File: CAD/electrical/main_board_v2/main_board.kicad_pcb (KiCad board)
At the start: 2 copper layers, 85.7 x 55.2 mm, 45 parts, among them J1 Battery in, J10 I2C Motor, J11 JTAG, J12 UART PGM, J2 Raspberry_Pi_2_3_4, J3 Trigger, J4 Side select, J5 Button A, J6 Button B, J7 I2C Peripheral, J8 I2C Peripheral, J9 I2C Motor, SW1 RESET, SW2 BOOT, U1 LM2576S-5, U2 AMS1117-3.3, U3 ESP32-WROOM-32, U4 PCA9306DC1, U5 PCA9306DC1, U6 MPU-6050

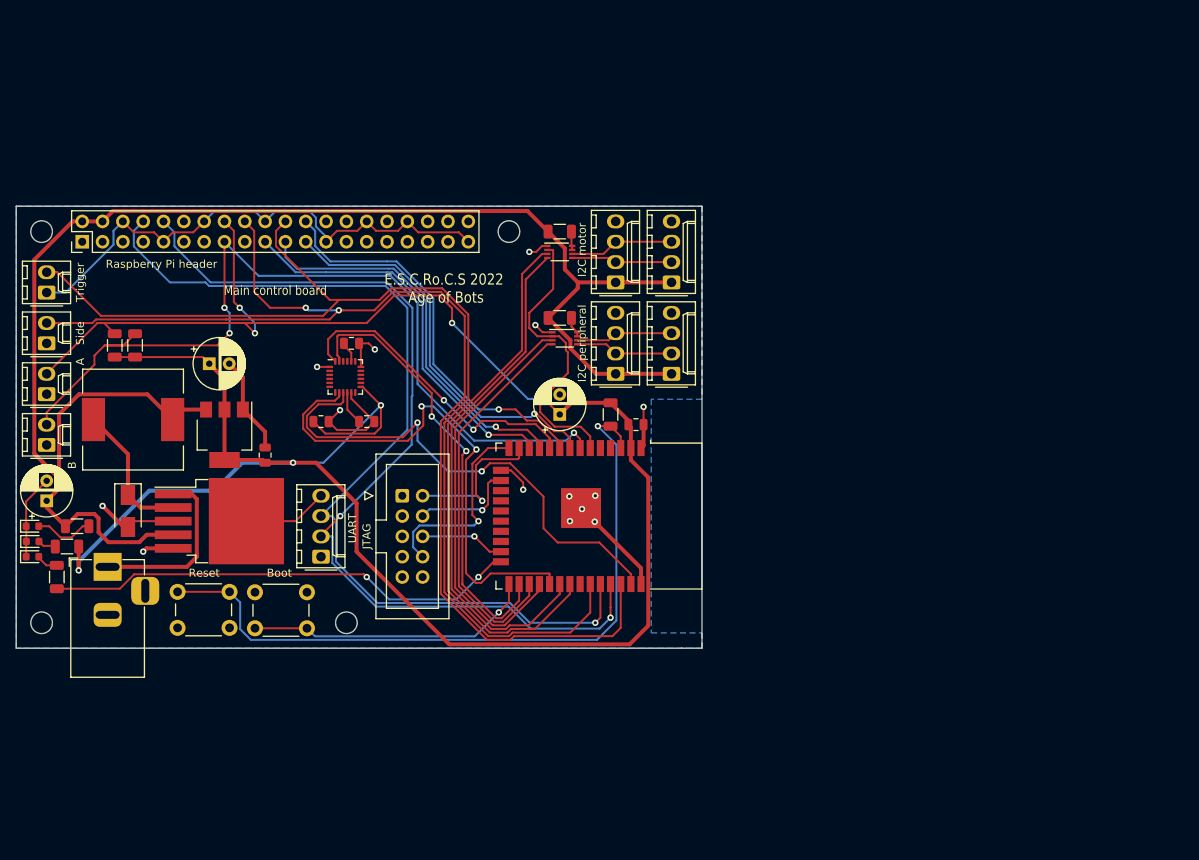
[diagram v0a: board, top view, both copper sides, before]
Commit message: Updated version of motor board and main board
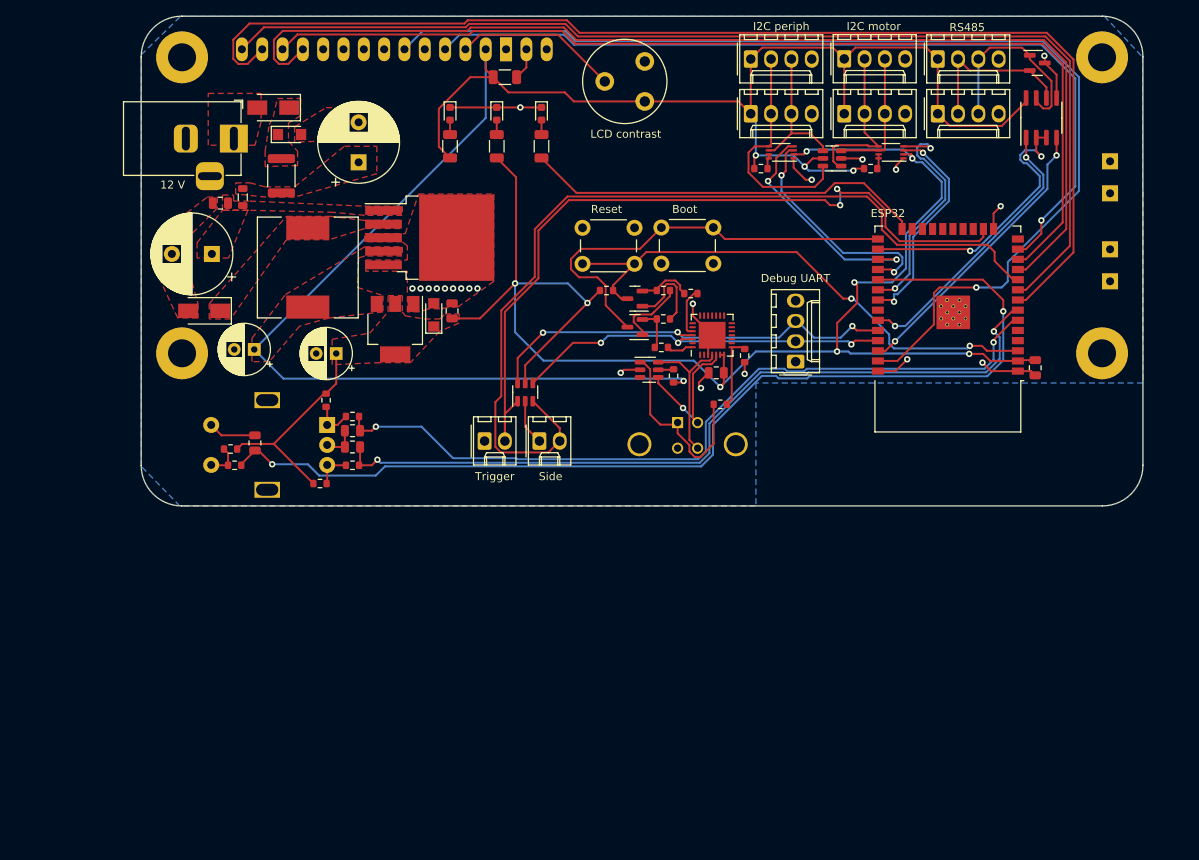
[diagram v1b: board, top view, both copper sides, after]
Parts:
- removed C1, C2, C5: 10u, Capacitor_THT:CP_Radial_D6.3mm_P2.50mm
- removed C3, C6, C7: 100n, Capacitor_SMD:C_0805_2012Metric
- removed C8: 2.2n 50V, Capacitor_SMD:C_0805_2012Metric
- removed D1: SS54, Diode_SMD:D_SMA
- removed D2: 5V power, LED_SMD:LED_0603_1608Metric
- removed D3: 3V3 power, LED_SMD:LED_0603_1608Metric
- removed J11: JTAG, Connector_IDC:IDC-Header_2x05_P2.54mm_Vertical
- removed J12: UART PGM, Connector_Molex:Molex_KK-254_AE-6410-04A_1x04_P2.54mm_Vertical
- removed J2: Raspberry_Pi_2_3_4, Connector_PinHeader_2.54mm:PinHeader_2x20_P2.54mm_Vertical
- removed J5: Button A, Connector_Molex:Molex_KK-254_AE-6410-02A_1x02_P2.54mm_Vertical
- removed J6: Button B, Connector_Molex:Molex_KK-254_AE-6410-02A_1x02_P2.54mm_Vertical
- removed L1: 100u, Inductor_SMD:L_12x12mm_H6mm
- removed R2, R7, R8: 10k, Resistor_SMD:R_1206_3216Metric
- removed R3: 100, Resistor_SMD:R_1206_3216Metric
- removed REF** (x4): MountingHole_2.7mm_M2.5, MountingHole:MountingHole_2.7mm_M2.5
- removed SW1: RESET, Button_Switch_THT:SW_PUSH_6mm
- removed SW2: BOOT, Button_Switch_THT:SW_PUSH_6mm
- removed U1: LM2576S-5, Package_TO_SOT_SMD:TO-263-5_TabPin3
- removed U2: AMS1117-3.3, Package_TO_SOT_SMD:SOT-223-3_TabPin2
- removed U6: MPU-6050, Sensor_Motion:InvenSense_QFN-24_4x4mm_P0.5mm
- added C12: 100n, Capacitor_SMD:C_0805_2012Metric, F.Cu at (83.3, 69.3)
- added C13: 100n, Capacitor_SMD:C_0805_2012Metric, F.Cu at (83.3, 71.4)
- added C14: 100n, Capacitor_SMD:C_0805_2012Metric, F.Cu at (71.1, 70.9)
- added C201: 100u, Capacitor_THT:CP_Radial_D10.0mm_P5.00mm, F.Cu at (84.1, 35.8)
- added C202: 100u, Capacitor_THT:CP_Radial_D10.0mm_P5.00mm, F.Cu at (65.7, 47.2)
- added C203: 100n, Capacitor_SMD:C_0805_2012Metric, F.Cu at (66.8, 40.9)
- added C204: 10u, Capacitor_THT:CP_Radial_D6.3mm_P2.50mm, F.Cu at (71.0, 59.2)
- added C205: 10u, Capacitor_THT:CP_Radial_D6.3mm_P2.50mm, F.Cu at (81.3, 59.7)
- added C206: 100n, Capacitor_SMD:C_0805_2012Metric, F.Cu at (95.8, 54.4)
- added C301: 100n, Capacitor_SMD:C_0805_2012Metric, F.Cu at (128.8, 62.1)
- added D201: SS54, Diode_SMD:D_SMA, F.Cu at (73.4, 29.0)
- added D202: SMF30A, Diode_SMD:D_SMF, F.Cu at (75.4, 32.3)
- added D203: SS54, Diode_SMD:D_SMA, F.Cu at (64.8, 54.4)
- added D204: 5V power, LED_SMD:LED_0603_1608Metric, F.Cu at (95.5, 29.7)
- added D205: 3V3 power, LED_SMD:LED_0603_1608Metric, F.Cu at (101.3, 29.7)
- added D206: SMF30A, Diode_SMD:D_SMF, F.Cu at (93.5, 54.9)
- added D8: PSM712, Package_TO_SOT_SMD:SOT-23, F.Cu at (168.9, 23.4)
- added F201: Polyfuse, Fuse:Fuse_1812_4532Metric, F.Cu at (74.4, 37.5)
- added FB201: FerriteBead, Inductor_SMD:L_0805_2012Metric, F.Cu at (69.6, 40.1)
- added J13: RS485, Connector_Molex:Molex_KK-254_AE-6410-04A_1x04_P2.54mm_Vertical, F.Cu at (156.5, 22.9)
- added J14: RS485, Connector_Molex:Molex_KK-254_AE-6410-04A_1x04_P2.54mm_Vertical, F.Cu at (156.5, 29.7)
- added J301: USB_B, Connector_USB:USB_B_TE_5787834_Vertical, B.Cu at (124.0, 68.3)
- added J302: UART PGM, Connector_Molex:Molex_KK-254_AE-6410-04A_1x04_P2.54mm_Vertical, F.Cu at (138.7, 60.7)
- added L201: 100u, Inductor_SMD:L_12x12mm_H6mm, F.Cu at (77.7, 48.9)
- added Q301: Q_NPN_BEC, Package_TO_SOT_SMD:SOT-23, F.Cu at (118.6, 56.4)
- added Q302: Q_NPN_BEC, Package_TO_SOT_SMD:SOT-23, F.Cu at (118.6, 52.8)
- added R10: 470, Resistor_SMD:R_0603_1608Metric, F.Cu at (83.3, 73.7)
- added R11: 10k, Resistor_SMD:R_0603_1608Metric, F.Cu at (79.2, 75.9)
- added R12: 10k, Resistor_SMD:R_0603_1608Metric, F.Cu at (80.0, 65.5)
- added R13: 10k, Resistor_SMD:R_0603_1608Metric, F.Cu at (68.1, 71.6)
- added R14: 470, Resistor_SMD:R_0603_1608Metric, F.Cu at (68.6, 73.7)
- added R201: 300, Resistor_SMD:R_1206_3216Metric, F.Cu at (95.5, 33.8)
- added R202: 100, Resistor_SMD:R_1206_3216Metric, F.Cu at (101.3, 33.8)
- added R301: 47k, Resistor_SMD:R_0603_1608Metric, F.Cu at (132.3, 59.9)
- added R302: 24k, Resistor_SMD:R_0603_1608Metric, F.Cu at (129.3, 66.0)
- added R303: 10k, Resistor_SMD:R_0603_1608Metric, F.Cu at (122.2, 51.8)
- added R304: 10k, Resistor_SMD:R_0603_1608Metric, F.Cu at (122.2, 55.4)
- added R305: 10k, Resistor_SMD:R_0603_1608Metric, F.Cu at (115.1, 51.8)
- added R306: 10k, Resistor_SMD:R_0603_1608Metric, F.Cu at (123.4, 62.5)
- added R307: 100, Resistor_SMD:R_0603_1608Metric, F.Cu at (125.6, 52.2)
- added R308: 100, Resistor_SMD:R_0603_1608Metric, F.Cu at (121.9, 58.9)
- added R9: 470, Resistor_SMD:R_0603_1608Metric, F.Cu at (83.3, 67.6)
- added RV1: LCD contrast, Potentiometer_THT:Potentiometer_Piher_PT-10-V05_Vertical, F.Cu at (119.8, 23.2)
- added SW3: Input encoder, Rotary_Encoder:RotaryEncoder_Alps_EC11E-Switch_Vertical_H20mm, B.Cu at (80.1, 68.6)
- added SW301: BOOT, Button_Switch_THT:SW_PUSH_6mm, F.Cu at (121.9, 43.9)
- added SW302: RESET, Button_Switch_THT:SW_PUSH_6mm, F.Cu at (112.1, 44.0)
- added U11: SRV05-4, Package_TO_SOT_SMD:SOT-23-6, F.Cu at (143.3, 35.3)
- added U201: LM2576S-5, Package_TO_SOT_SMD:TO-263-5_TabPin3, F.Cu at (93.0, 45.2)
- added U202: AMS1117-3.3, Package_TO_SOT_SMD:SOT-223-3_TabPin2, F.Cu at (88.6, 56.6)
- added U301: SRV05-4, Package_TO_SOT_SMD:SOT-23-6, F.Cu at (120.4, 61.7)
- added U302: CP2102N-Axx-xQFN28, Package_DFN_QFN:QFN-28-1EP_5x5mm_P0.5mm_EP3.35x3.35mm, F.Cu at (128.3, 57.4)
- added U7: LCD-016N002L, Display:LCD-016N002L, B.Cu at (102.5, 21.7)
- added U8: MAX485E, Package_SO:SOIC-8_3.9x4.9mm_P1.27mm, F.Cu at (169.4, 30.2)
- added U9: SRV05-4, Package_TO_SOT_SMD:SOT-23-6, F.Cu at (104.9, 64.5)
- R1: value 300 -> 470
- R5, R6: footprint Resistor_SMD:R_1206_3216Metric -> Resistor_SMD:R_0603_1608Metric
- moved D4 84.3 mm to (106.9, 29.7), turned to -90 degrees
- moved R4 81.1 mm to (106.9, 33.8)
- moved R1 77.5 mm to (102.4, 25.1), turned to 180 degrees
- moved J4 62.8 mm to (106.7, 70.6), turned to 0 degrees
- moved J3 57.8 mm to (99.8, 70.6), turned to 0 degrees
- moved J1 55.8 mm to (68.5, 32.8), turned to 0 degrees
- moved U3 53.6 mm to (157.7, 53.6), turned to 180 degrees
- moved C4 50.4 mm to (168.7, 61.5), turned to -90 degrees
- moved U5 43.2 mm to (150.6, 34.5), turned to 180 degrees
- moved J8 42.8 mm to (133.1, 22.9), turned to 0 degrees
- moved R6 39.7 mm to (148.1, 36.6)
- moved U4 35.7 mm to (136.9, 34.5), turned to 180 degrees
- moved J9 35.5 mm to (144.8, 29.7), turned to 0 degrees
- moved J10 35.3 mm to (144.8, 22.9), turned to 0 degrees
- moved J7 34.0 mm to (133.1, 29.7), turned to 0 degrees
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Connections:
- J1 pad 1: Net-(J1-Pad1) -> /Power supply/12V_in
- R1 pad 1: +5V -> Net-(R1-Pad1)
- R1 pad 2: Net-(D2-Pad2) -> +5V
- U3 pad 10: /SPI2_MOSI -> /SIDE_BTN
- U3 pad 11: /SPI_MISO -> /LCD_DB4
- U3 pad 12: /SPI_MOSI -> /LCD_DB5
- U3 pad 13: /JTAG_TMS -> /LCD_RS
- U3 pad 14: /JTAG_TDI -> unconnected-(U3-Pad14)
- U3 pad 16: /JTAG_TCK -> /TRIG_BTN
- U3 pad 17: Net-(U3-Pad17) -> unconnected-(U3-Pad17)
- U3 pad 18: Net-(U3-Pad18) -> unconnected-(U3-Pad18)
- U3 pad 19: Net-(U3-Pad19) -> unconnected-(U3-Pad19)
- U3 pad 20: Net-(U3-Pad20) -> unconnected-(U3-Pad20)
- U3 pad 21: Net-(U3-Pad21) -> unconnected-(U3-Pad21)
- U3 pad 22: Net-(U3-Pad22) -> unconnected-(U3-Pad22)
- U3 pad 23: /JTAG_TDO -> unconnected-(U3-Pad23)
- U3 pad 25: Net-(SW2-Pad2) -> /BOOT
- U3 pad 26: /SPI2_CLK -> /RS485_TXE
- U3 pad 29: /SPI2_CS0 -> /INPUT_SW
- U3 pad 3: Net-(R2-Pad2) -> /RESET
- U3 pad 32: Net-(U3-Pad32) -> unconnected-(U3-Pad32)
- U3 pad 33: /TRIG_BTN -> /UART2_RX
- U3 pad 36: /SIDE_BTN -> /UART2_TX
- U3 pad 37: /SPI2_MISO -> /LCD_E
- U3 pad 4: Net-(U3-Pad4) -> unconnected-(U3-Pad4)
- U3 pad 5: Net-(U3-Pad5) -> unconnected-(U3-Pad5)
- U3 pad 6: /BTN_A -> /INPUT_A
- U3 pad 7: /BTN_B -> /INPUT_B
- U3 pad 8: /SPI_CLK -> /LCD_DB6
- U3 pad 9: /SPI_CS0 -> /LCD_DB7
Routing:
- net /LCD_DB6: track 0.00 -> 148.6 mm
- net /LCD_E: track 0.00 -> 139.5 mm, vias 0 -> 1
- net /LCD_DB7: track 0.00 -> 138.6 mm
- net /LCD_DB4: track 0.00 -> 137.5 mm
- net /INPUT_SW: track 0.00 -> 129.5 mm, vias 0 -> 2
- net /LCD_DB5: track 0.00 -> 127.5 mm
- net /BTN_B: track 107.6 -> 0.00 mm, vias 3 -> 0
- net /LCD_RS: track 0.00 -> 106.7 mm, vias 0 -> 1
- net /BTN_A: track 102.9 -> 0.00 mm, vias 4 -> 0
- net /INPUT_B: track 0.00 -> 97.9 mm, vias 0 -> 2
- net /INPUT_A: track 0.00 -> 96.3 mm, vias 0 -> 2
- net GND: track 164.1 -> 69.8 mm, vias 14 -> 21
- net Net-(R2-Pad2): track 90.4 -> 0.00 mm, vias 1 -> 0
- net /UART_MISO: track 117.6 -> 48.4 mm, vias 2 -> 3
- net /RESET: track 0.00 -> 67.7 mm, vias 0 -> 2
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- added copper zone on F.Cu, net +12V
- added copper zone on F.Cu, net +3V3
- added copper zone on F.Cu, net +5V
- added copper zone on F.Cu, net /Power supply/12V_in
- added copper zone on F.Cu, net GND
- added copper zone on F.Cu, net Net-(C201-Pad1)
- added copper zone on F.Cu, net Net-(D201-Pad1)
- added copper zone on F.Cu, net Net-(D203-Pad1)
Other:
- board size 85.7 x 55.2 mm -> 125.2 x 61.2 mm
- net class Default removed
- net class Power removed
- board text added: "12 V"
- board text added: "Debug UART"
- board text added: "ESP32"
- board text added: "I2C periph"
- board text added: "LCD contrast"
- board text added: "RS485"
- board text added: "Rotary encoder"
- board text added: "USB"
- board text removed: "A"
- board text removed: "B"
- board text removed: "E.S.C.Ro.C.S 2022 ~ Age of Bots ~"
- board text removed: "I2C peripheral"
- board text removed: "JTAG"
- board text removed: "Main control board"
- board text removed: "Raspberry Pi header"
- board text removed: "UART"

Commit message: Kicad CAD for mainboard and motorboard (final)
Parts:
- removed J302: UART PGM, Connector_Molex:Molex_KK-254_AE-6410-04A_1x04_P2.54mm_Vertical
- added C1: 100u, Capacitor_SMD:CP_Elec_8x10, F.Cu at (142.0, 100.1)
- added C2: 100n, Capacitor_SMD:C_0805_2012Metric, F.Cu at (136.3, 103.6)
- added J2: UART PGM, Connector_Molex:Molex_KK-254_AE-6410-04A_1x04_P2.54mm_Vertical, B.Cu at (154.1, 109.6)
- added L1: 10u, Inductor_SMD:L_12x12mm_H6mm, F.Cu at (129.3, 112.3)
- added R2: 1k, Resistor_SMD:R_0603_1608Metric, F.Cu at (140.7, 105.7)
- added R3: 1k, Resistor_SMD:R_0603_1608Metric, F.Cu at (145.8, 105.8)
- C201, C202: footprint Capacitor_THT:CP_Radial_D10.0mm_P5.00mm -> Capacitor_SMD:CP_Elec_8x10
- C204: value 10u -> 2000u; footprint Capacitor_THT:CP_Radial_D6.3mm_P2.50mm -> Capacitor_SMD:CP_Elec_10x10.5
- C205: value 10u -> 100u; footprint Capacitor_THT:CP_Radial_D6.3mm_P2.50mm -> Capacitor_SMD:CP_Elec_8x10
- R1: value 470 -> 300
- R10, R14, R9: value 470 -> 620
- R202, R4: value 100 -> 300
- R301: value 47k -> 82k
- R302: value 24k -> 36k
- R5, R6: value 100k -> 33k
- RV1: footprint Potentiometer_THT:Potentiometer_Piher_PT-10-V05_Vertical -> Potentiometer_SMD:Potentiometer_Bourns_3314J_Vertical
- SW301, SW302: footprint Button_Switch_THT:SW_PUSH_6mm -> Button_Switch_SMD:SW_Push_1P1T_NO_6x6mm_H9.5mm; moved to B.Cu
- U3: footprint RF_Module:ESP32-WROOM-32 -> RF_Module:ESP32-WROOM-32U; moved to B.Cu
- U7: footprint Display:LCD-016N002L -> Display:WC1602A
- moved D4 104.4 mm to (185.8, 98.2), turned to 90 degrees
- moved D205 103.9 mm to (179.5, 98.2), turned to 90 degrees
- moved D204 103.5 mm to (173.1, 98.2), turned to 90 degrees
- moved R4 99.0 mm to (182.6, 97.5), turned to 0 degrees
- moved R202 98.4 mm to (176.3, 97.5), turned to 0 degrees
- moved R201 98.0 mm to (169.9, 97.5), turned to 0 degrees
- moved J13 95.9 mm to (139.4, 117.2)
- moved U7 89.6 mm to (176.9, 71.5)
- moved D8 86.1 mm to (151.5, 107.7), turned to -90 degrees
- moved SW301 84.1 mm to (164.2, 116.6), turned to 180 degrees
- moved SW302 83.8 mm to (164.2, 109.6), turned to 180 degrees
- moved J8 83.5 mm to (176.3, 94.4), turned to 90 degrees
- moved J14 82.3 mm to (139.4, 110.3)
- moved J7 81.8 mm to (183.3, 94.4), turned to 90 degrees
- moved R306 80.1 mm to (182.0, 117.2), turned to 180 degrees
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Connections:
- C204 pad 1: +5V -> Net-(C204-Pad1)
- L201 pad 2: +5V -> Net-(C204-Pad1)
- U201 pad 4: +5V -> Net-(C204-Pad1)
- U3 pad 34: /UART_MOSI -> /UART_RX
- U3 pad 35: /UART_MISO -> /UART_TX
- U302 pad 25: /UART_MOSI -> /UART_TX
- U302 pad 26: /UART_MISO -> /UART_RX
- U9 pad 4: /UART_MISO -> /UART_TX
- U9 pad 6: /UART_MOSI -> /UART_RX
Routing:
- net /LCD_DB6: track 148.6 -> 29.3 mm, vias 0 -> 1
- net /LCD_DB7: track 138.6 -> 29.4 mm, vias 0 -> 1
- net /LCD_E: track 139.5 -> 31.5 mm
- net /LCD_DB4: track 137.5 -> 29.6 mm, vias 0 -> 1
- net /LCD_DB5: track 127.5 -> 32.9 mm, vias 0 -> 1
- net /LCD_RS: track 106.7 -> 36.3 mm
- net /INPUT_SW: track 129.5 -> 71.5 mm, vias 2 -> 3
- net +5V: track 241.9 -> 186.0 mm, vias 4 -> 0
- net /INPUT_A: track 96.3 -> 40.9 mm, vias 2 -> 1
- net /UART_MOSI: track 54.1 -> 0.00 mm, vias 3 -> 0
- net /INPUT_B: track 97.9 -> 48.4 mm, vias 2 -> 1
- net /UART_MISO: track 48.4 -> 0.00 mm, vias 3 -> 0
- net /UART_RX: track 0.00 -> 45.8 mm, vias 0 -> 1
- net /UART_TX: track 0.00 -> 37.2 mm, vias 0 -> 1
- net +3V3: track 210.7 -> 176.8 mm, vias 8 -> 7
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- added copper zone on F.Cu, net Net-(C204-Pad1)
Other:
- board size 125.2 x 61.2 mm -> 84.5 x 54.6 mm
- board text added: "12V in"
- board text added: "BOOT"
- board text added: "I2C Motor"
- board text added: "I2C peripheral"
- board text added: "Les E.S.C.Ro.C.S. CPU board 2024 ~ Farming Mars"
- board text added: "RESET"
- board text added: "UART flash"
- board text removed: "12 V"
- board text removed: "Boot"
- board text removed: "Debug UART"
- board text removed: "ESP32"
- board text removed: "I2C motor"
- board text removed: "I2C periph"
- board text removed: "LCD contrast"
- board text removed: "Reset"
- board text removed: "Rotary encoder"
